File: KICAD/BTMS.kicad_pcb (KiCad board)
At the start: 4 copper layers, 126.2 x 137.4 mm, 316 parts, among them J1 fan, J10 U1COMMS, J11 U2COMMS, J13 IntBTemp, J14 ctrlTemp, J15 12Vout, J16 12Vin, J17 5Vout, J2 mContactor, J3 Tac, J5 ICSP, J7 5Vout, J9 key, Q1 PSMN5R6-100BS, Q10 PSMN5R6-100BS, Q11 DMN65D8L, Q12 DMN65D8L, Q13 FDN340P, Q14 ZXTP2025FTA, Q15 ZXTP2025FTA, Q16 ZXTP2025FTA, Q17 DMN65D8L, Q18 DMN65D8L, Q2 PSMN5R6-100BS, Q3 PSMN5R6-100BS, Q4 DMN65D8L, Q5 DMN65D8L, Q6 DMN65D8L, Q7 DMN65D8L, Q8 PSMN5R6-100BS, Q9 FDN340P, U1 R-78HB12-0.5, U10 A41AS12VDC, U11 A41AS12VDC, U12 A41AS12VDC, U13 A41AS12VDC, U14 A41AS12VDC, U15 NL17SZ74USG, U2 ACS780xLRTR-050B, U3 UCC27201DDAR, U4 FAN3111ESX, U5 HCPL-3120, U6 L7805CV, U7 LTV-817S, U8 dsPIC30F3011-PT, U9 LM62CIM3/NOPB

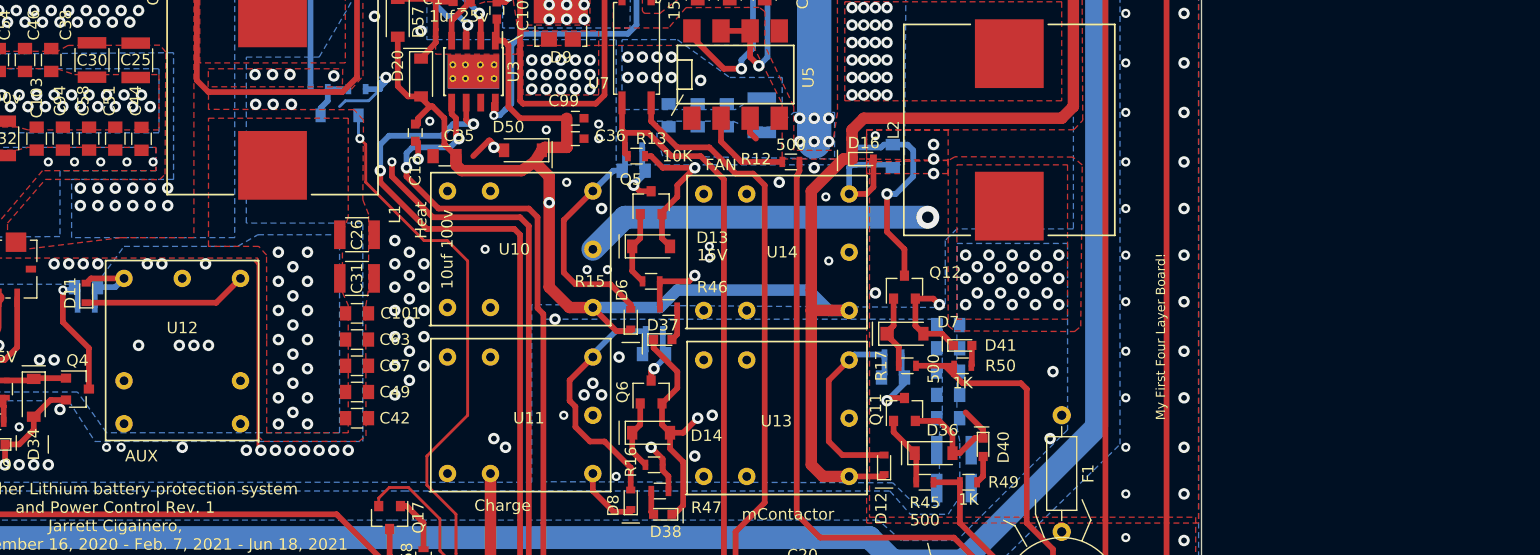
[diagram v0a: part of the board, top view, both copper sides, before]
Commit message: Began board design bug fixes and upgrades. Began implementing vehicle speed calculation routines. Fixed a bug where system would power itself off 1 sec after unplugging charger. Fixed a bug where heater relay would not turn on/off during heat test and cal. Fixed a bug where AUX and mContactor relays would not turn on. Fixed a bug where system would hang when attempting to read fault codes.
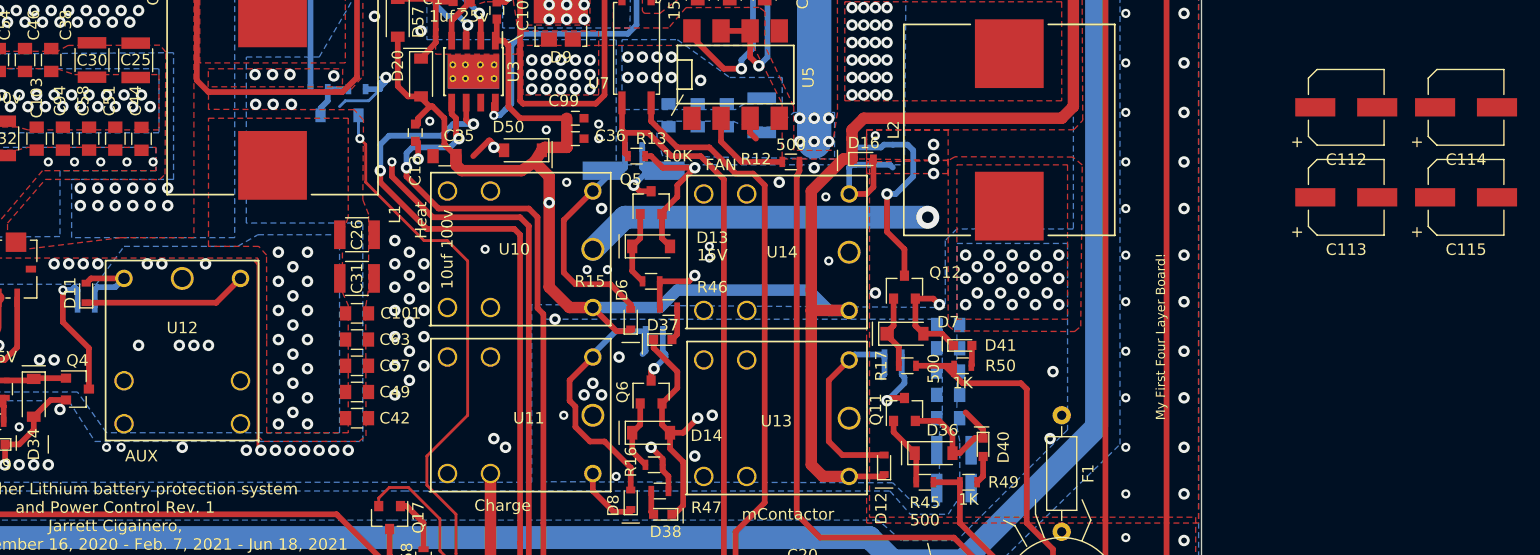
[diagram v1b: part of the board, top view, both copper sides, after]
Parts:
- C111: value 10uf 25v -> 100uf 16v; footprint Capacitors_SMD:C_0805 -> Capacitors_SMD:CP_Elec_6.3x5.7
- C112, C113, C114, C115: value 10uf 25v -> 100uf 16v; footprint Capacitors_SMD:C_0805 -> Capacitors_SMD:CP_Elec_6.3x5.7; moved to F.Cu
- moved C113 110.2 mm to (169.9, 98.3), turned to 0 degrees
- moved C112 64.1 mm to (169.9, 90.5)
- moved C114 55.3 mm to (180.3, 90.5)
- moved C115 50.1 mm to (180.3, 98.3), turned to 0 degrees

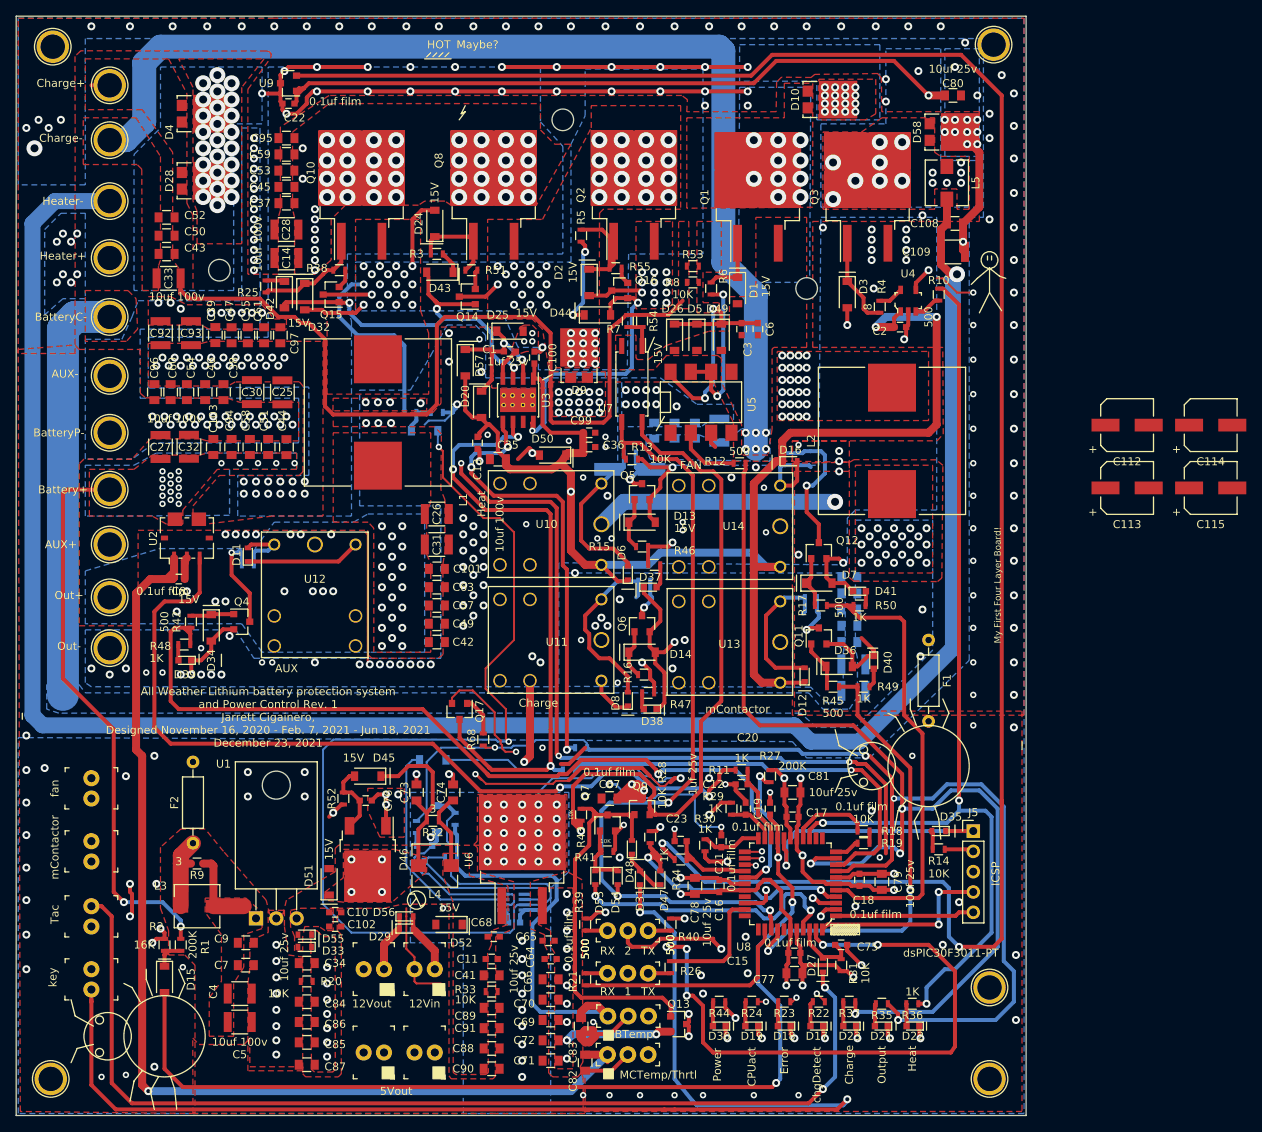
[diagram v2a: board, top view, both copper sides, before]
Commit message: Updated readme to list current state of project.
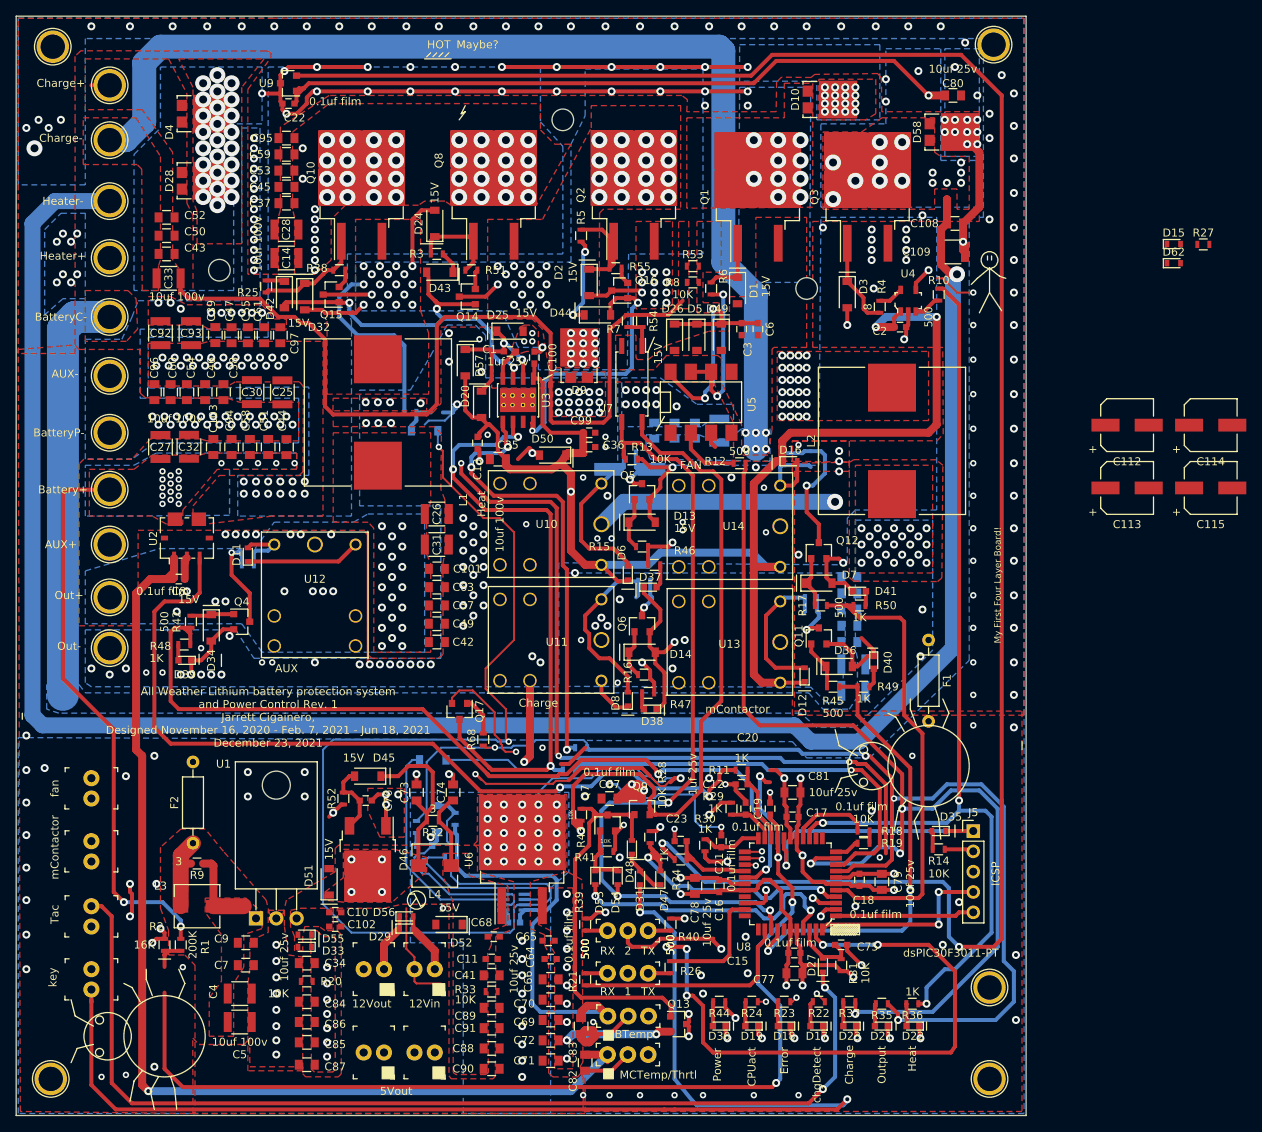
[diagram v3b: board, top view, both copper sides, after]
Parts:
- removed L5: 10uH, Inductors:Inductor_Wurth_HCI-5040
- removed R58: 16K, Resistors_SMD:R_0603
- added D62: Diode40V, Diodes_SMD:D_0603, F.Cu at (175.7, 70.2)
- D15: value D_Schottky100V -> Diode40V; footprint Diodes_SMD:D_SOD-123 -> Diodes_SMD:D_0603
- R27: value 200K -> 1K
- moved D15 156.1 mm to (175.7, 67.9), turned to 0 degrees
- moved R27 85.7 mm to (179.4, 67.9), turned to 0 degrees
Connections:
- D15 pad 1: Net-(D15-Pad1) -> +5C
- R1 pad 1: Net-(D15-Pad1) -> Net-(R1-Pad1)
- R2 pad 2: Net-(D15-Pad1) -> Net-(R1-Pad1)
- R27 pad 1: /BVsense -> Net-(R1-Pad1)
- R27 pad 2: +5C -> /BVsense
- U4 pad 4: +5P -> +5C
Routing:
- net Net-(R1-Pad1): track 0.00 -> 4.80 mm
- net Net-(D15-Pad1): track 4.80 -> 0.00 mm
- net +5C: track 364.5 -> 367.7 mm, vias 13 -> 14
- net +5P: track 3.12 -> 0.00 mm, vias 1 -> 0
